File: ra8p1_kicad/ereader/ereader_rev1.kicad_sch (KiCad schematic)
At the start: 0 parts

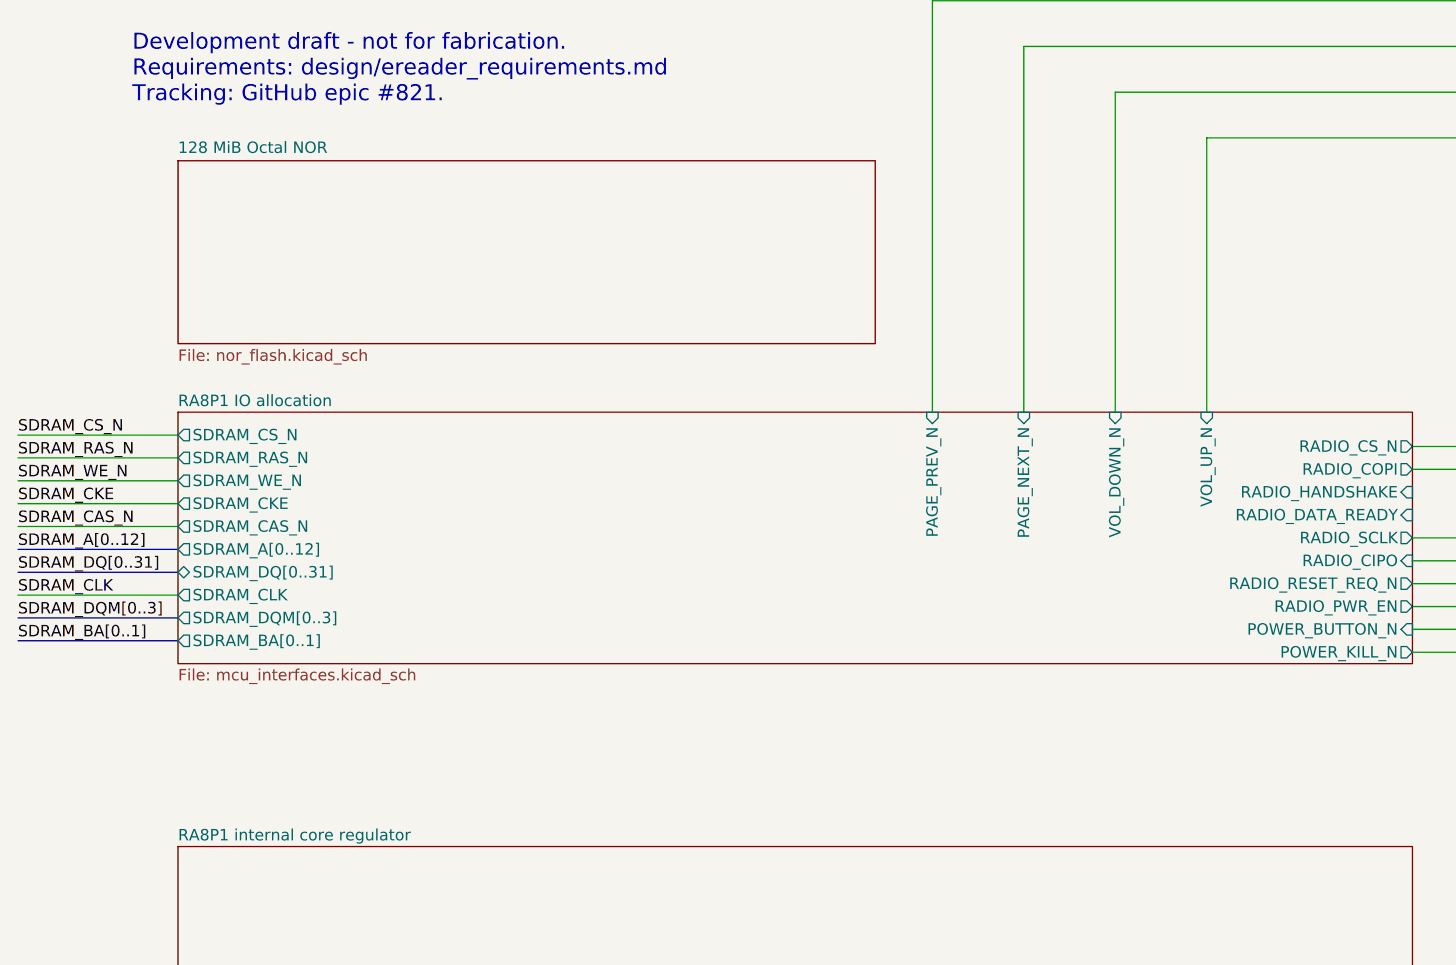
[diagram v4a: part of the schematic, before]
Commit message: Connect Octal NOR hierarchy and configured MCU pins
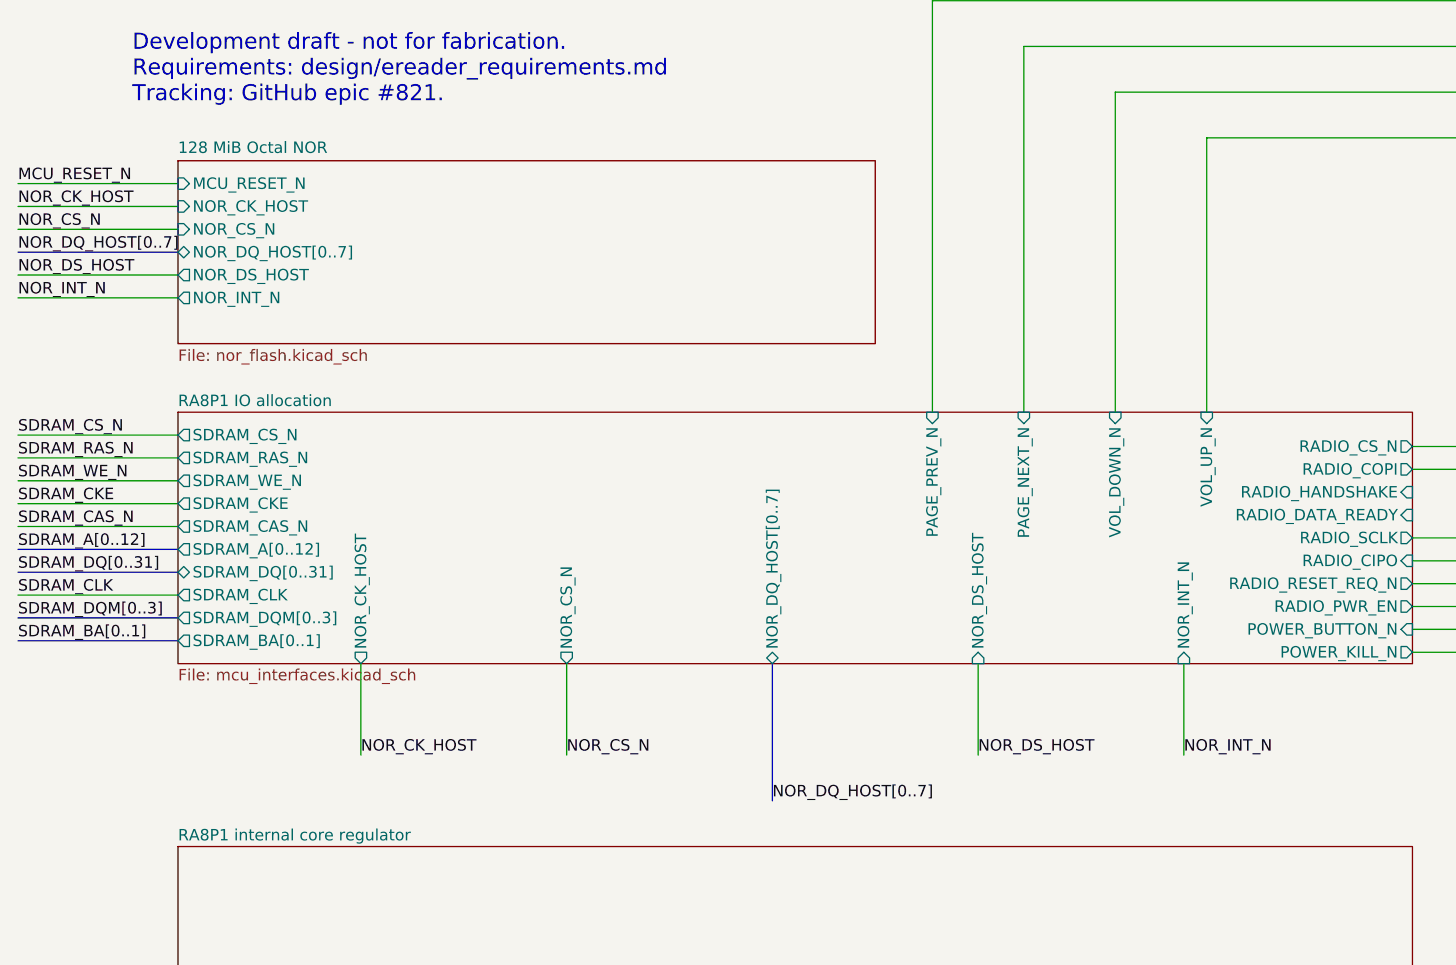
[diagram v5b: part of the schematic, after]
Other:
- sheet 128 MiB Octal NOR ports: added MCU_RESET_N, NOR_CK_HOST, NOR_CS_N, NOR_DQ_HOST[0..7], NOR_DS_HOST, NOR_INT_N; removed none
- sheet RA8P1 IO allocation ports: added NOR_CK_HOST, NOR_CS_N, NOR_DQ_HOST[0..7], NOR_DS_HOST, NOR_INT_N; removed none

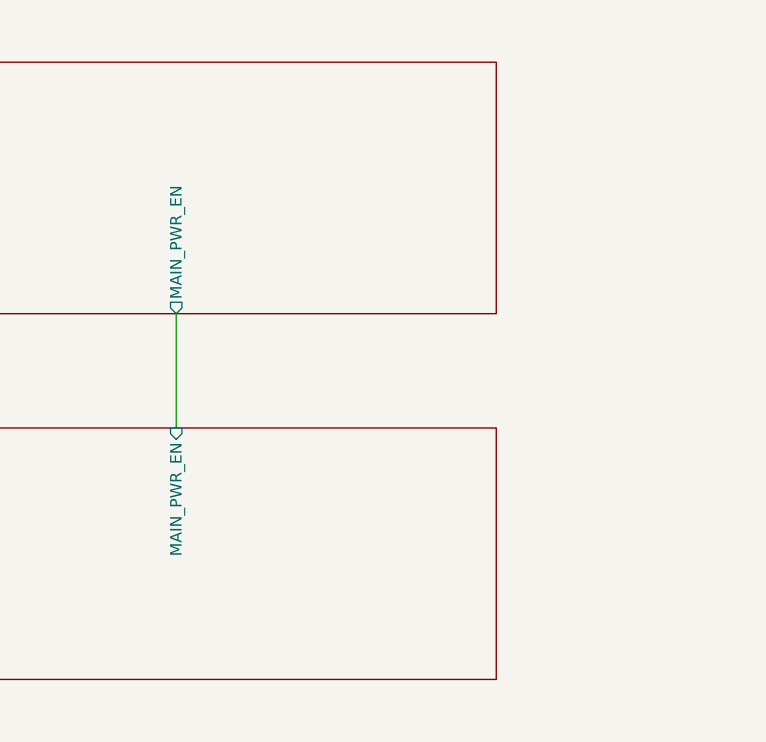
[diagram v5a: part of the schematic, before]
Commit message: Wire LTC3119 power-stage draft and held RUN control
Add native RUN buffer and held-domain clamp with verified connectivity, sourced BOM fields, and linked PWR-004 calculations. Export the full schematic PDF and native BOM.

Keep rail adoption blocked by SDRAM logic-high conflict #846. Whole-project ERC remains 133 errors and two warnings; this checkpoint adds no findings.
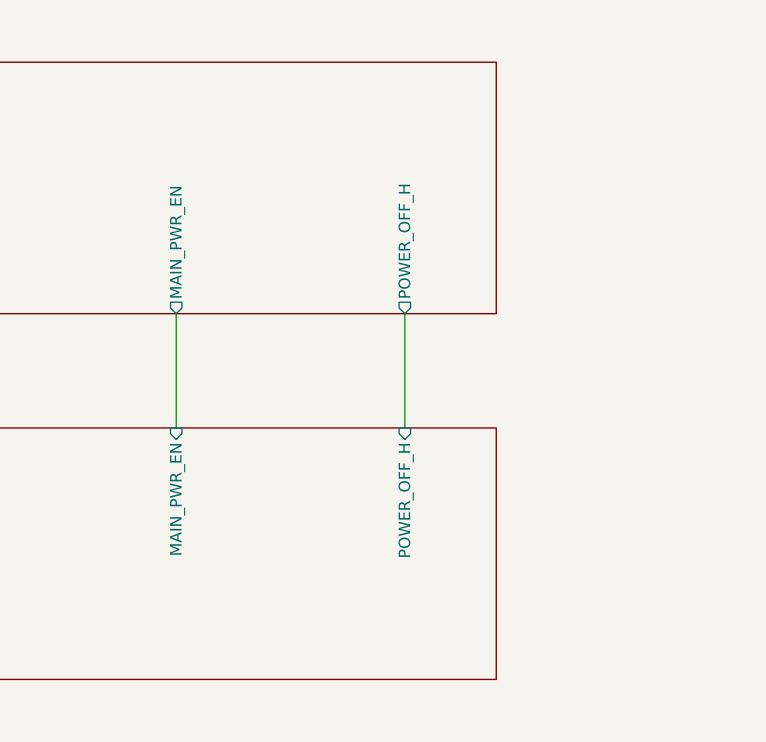
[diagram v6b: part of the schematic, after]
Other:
- sheet Main 3V3 digital supply ports: added POWER_OFF_H; removed none
- sheet Power button and source control ports: added POWER_OFF_H; removed none
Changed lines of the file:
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@@
+	(wire
+		(pts
+			(xy 330.2 205.74) (xy 330.2 218.44)
+		)
+		(stroke
+			(width 0)
+			(type default)
+		)
+	)
 	(wire
 		(pts
@@
 			)
 		)
+		(pin "POWER_OFF_H" input
+			(at 330.2 218.44 90)
+			(effects
+				(font
+					(size 1.27 1.27)
+				)
+				(justify right)
+			)
+		)
 		(instances
 			(project "ereader_rev1"
@@
 			(effects
 				(font
+					(size 1.27 1.27)
+				)
+				(justify left)
+			)
+		)
+		(pin "POWER_OFF_H" output
+			(at 330.2 205.74 270)
+			(effects
+				(font

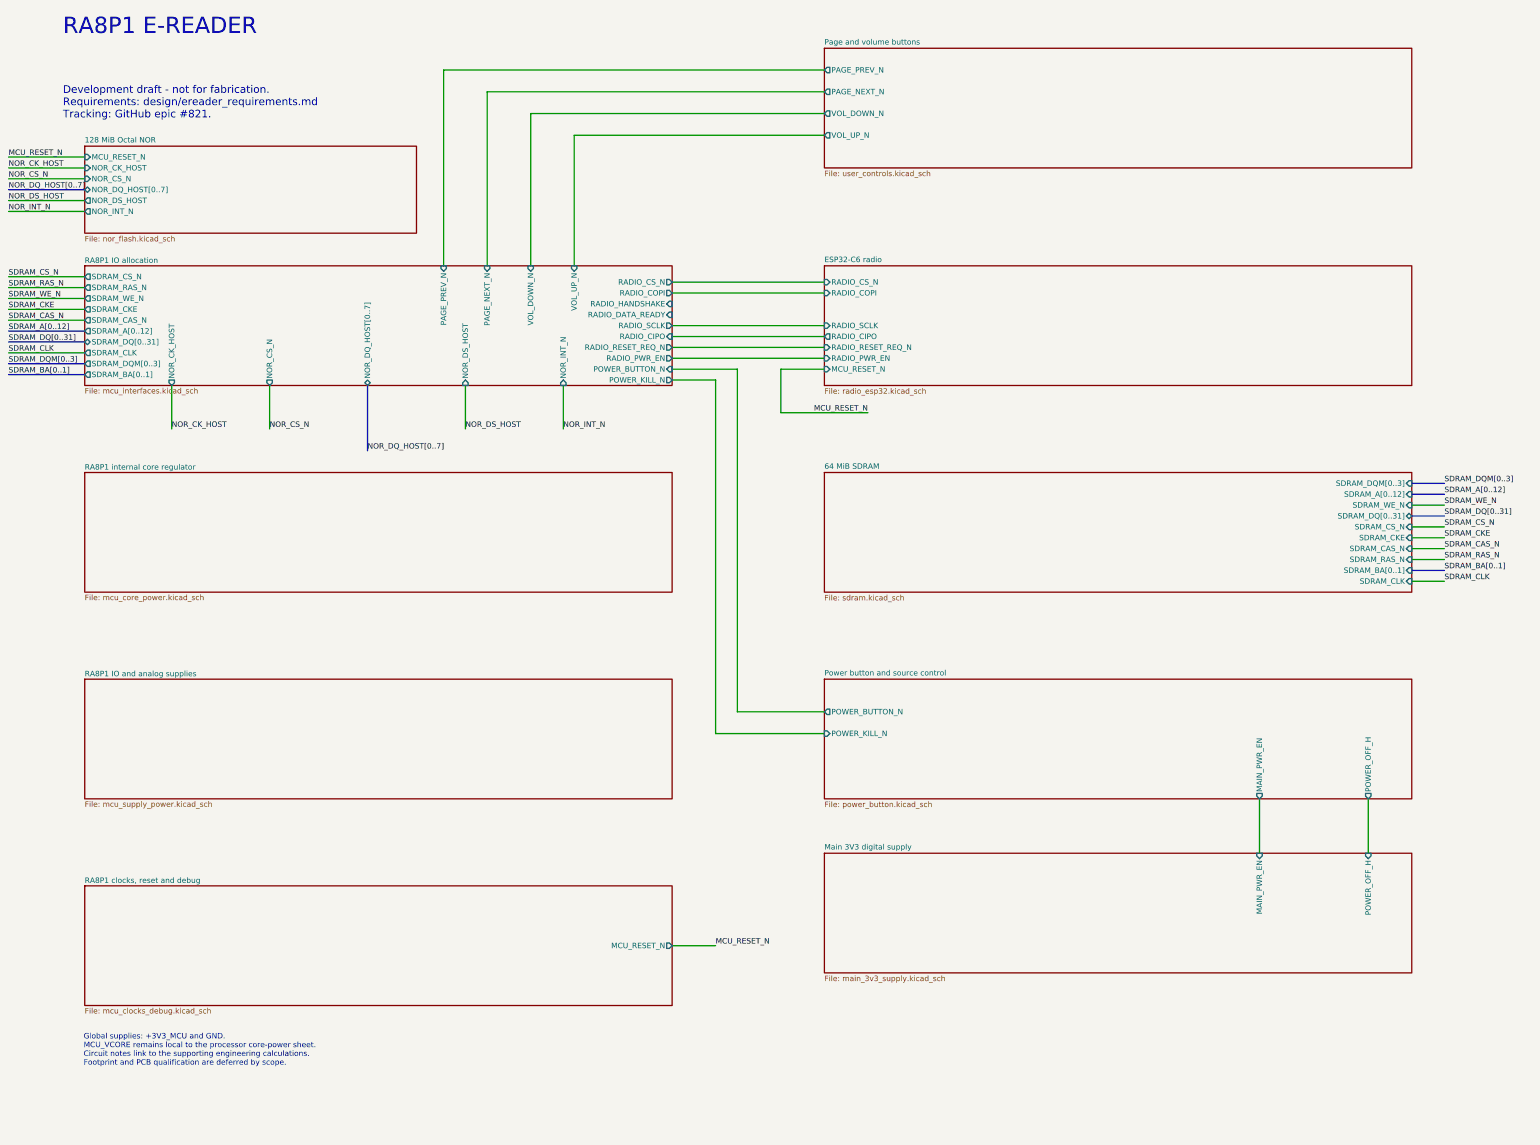
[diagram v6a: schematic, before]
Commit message: Add microSD socket and verified mechanical card detect
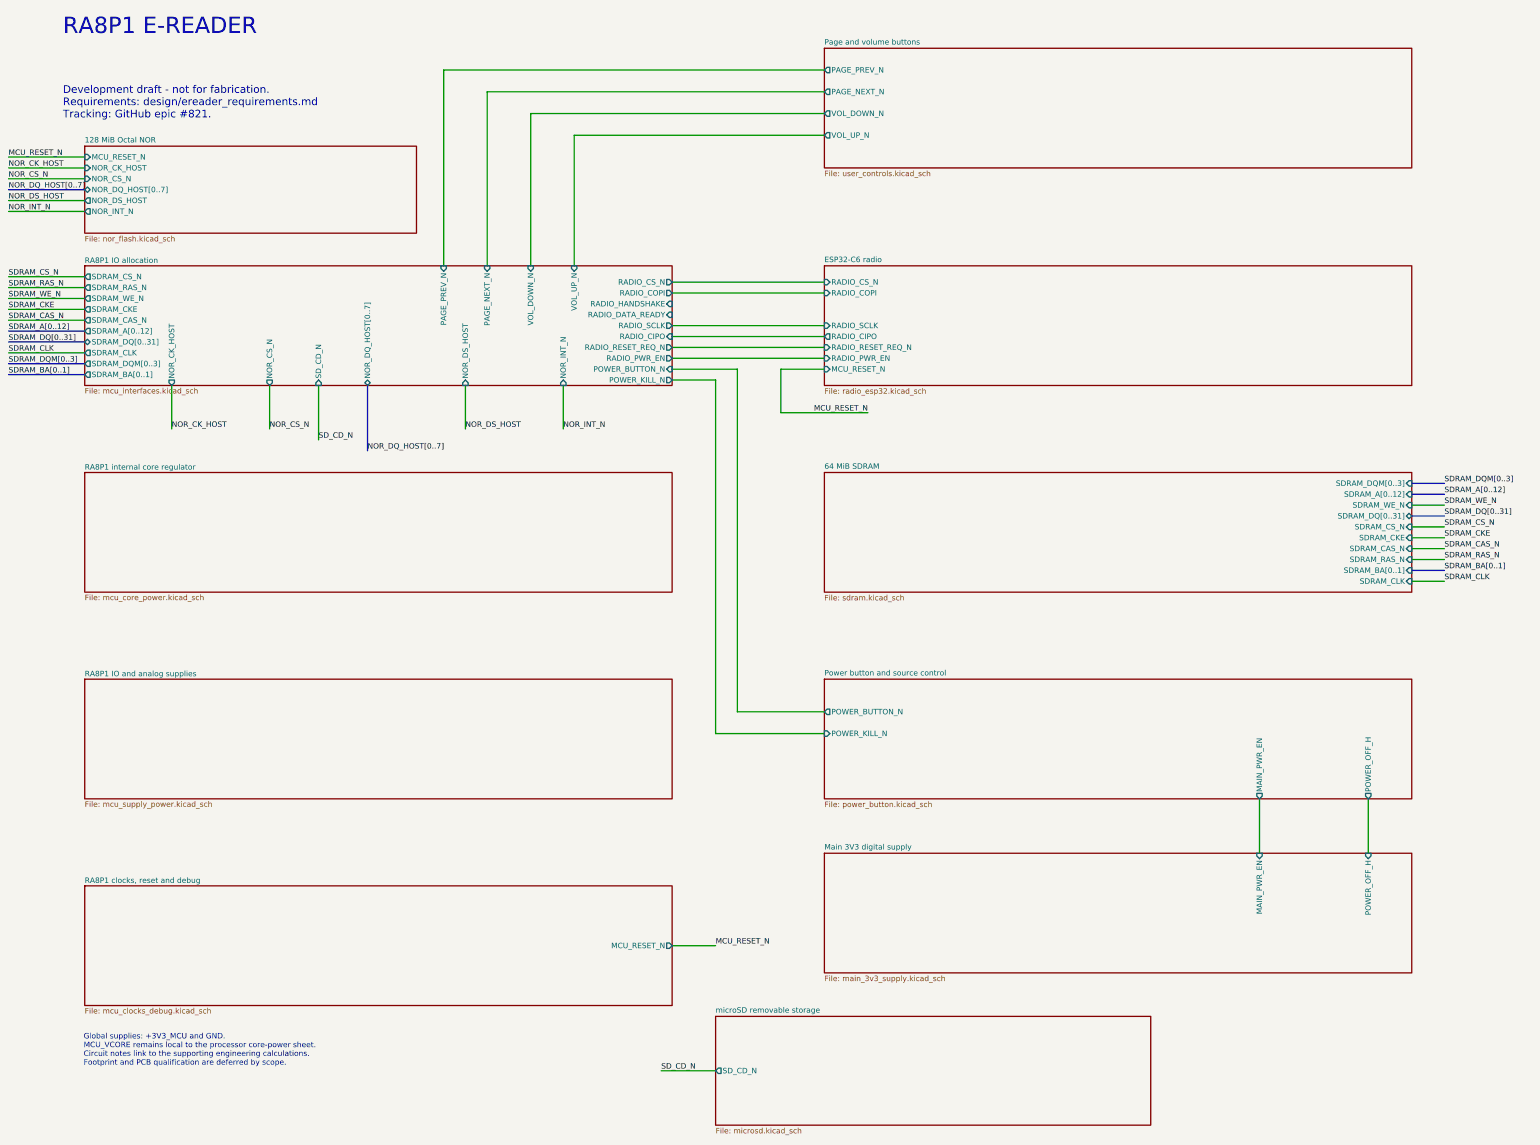
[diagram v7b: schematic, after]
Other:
- added sheet microSD removable storage (microsd.kicad_sch)
- sheet RA8P1 IO allocation ports: added SD_CD_N; removed none
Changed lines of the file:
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@@
+	(wire
+		(pts
+			(xy 85.09 109.22) (xy 85.09 121.92)
+		)
+		(stroke
+			(width 0)
+			(type default)
+		)
+	)
 	(wire
 		(pts
@@
 		(pts
 			(xy 12.7 58.42) (xy 30.48 58.42)
+		)
+		(stroke
+			(width 0)
+			(type default)
+		)
+	)
+	(wire
+		(pts
+			(xy 165.1 269.24) (xy 177.8 269.24)
 		)
 		(stroke
@@
 		)
 	)
+	(label "SD_CD_N"
+		(at 85.09 121.92 0)
+		(effects
+			(font
+				(size 1.27 1.27)
+			)
+			(justify left bottom)
+		)
+	)
 	(label "SDRAM_BA[0..1]"
 		(at 347.98 152.4 0)
@@
 	(label "SDRAM_DQM[0..3]"
 		(at 12.7 104.14 0)
+		(effects
+			(font
+				(size 1.27 1.27)
+			)
+			(justify left bottom)
+		)
+	)
+	(label "SD_CD_N"
+		(at 165.1 269.24 0)
 		(effects
 			(font
@@
 			)
 		)
+		(pin "SD_CD_N" input
+			(at 85.09 109.22 270)
+			(effects
+				(font
+					(size 1.27 1.27)
+				)
+				(justify left)
+			)
+		)
 		(instances
 			(project "ereader_rev1"
@@
 				)
 			)
+		)
+	)
+	(sheet
+		(at 177.8 256.54)
+		(size 101.6 25.4)
+		(exclude_from_sim no)
+		(in_bom yes)
+		(on_board yes)
+		(dnp no)
+		(fields_autoplaced yes)
+		(stroke
+			(width 0.1524)
+			(type solid)
+		)
+		(fill
+			(color 0 0 0 0)
+		)
+		(property "Sheetname" "microSD removable storage"
+			(at 177.8 255.8284 0)
+			(show_name no)
+			(do_not_autoplace no)
+			(effects
+				(font
+					(size 1.27 1.27)
+				)
+				(justify left bottom)
+			)
+		)
+		(property "Sheetfile" "microsd.kicad_sch"
+			(at 177.8 282.5246 0)
+			(show_name no)
+			(do_not_autoplace no)
+			(effects
+				(font
+					(size 1.27 1.27)
+				)
+				(justify left top)
+			)
+		)
+		(pin "SD_CD_N" output
+			(at 177.8 269.24 180)
+			(effects
+				(font
+					(size 1.27 1.27)
+				)
+				(justify left)
+			)
+		)
+		(instances
+			(project "ereader_rev1"
+				(path "/0586cc51-9c57-495b-a0c9-c29ba0d48166"
+					(page "12")
+				)
+			)

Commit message: hardware: integrate supervised microSD power and SDHI bus (#827, #845, #846)
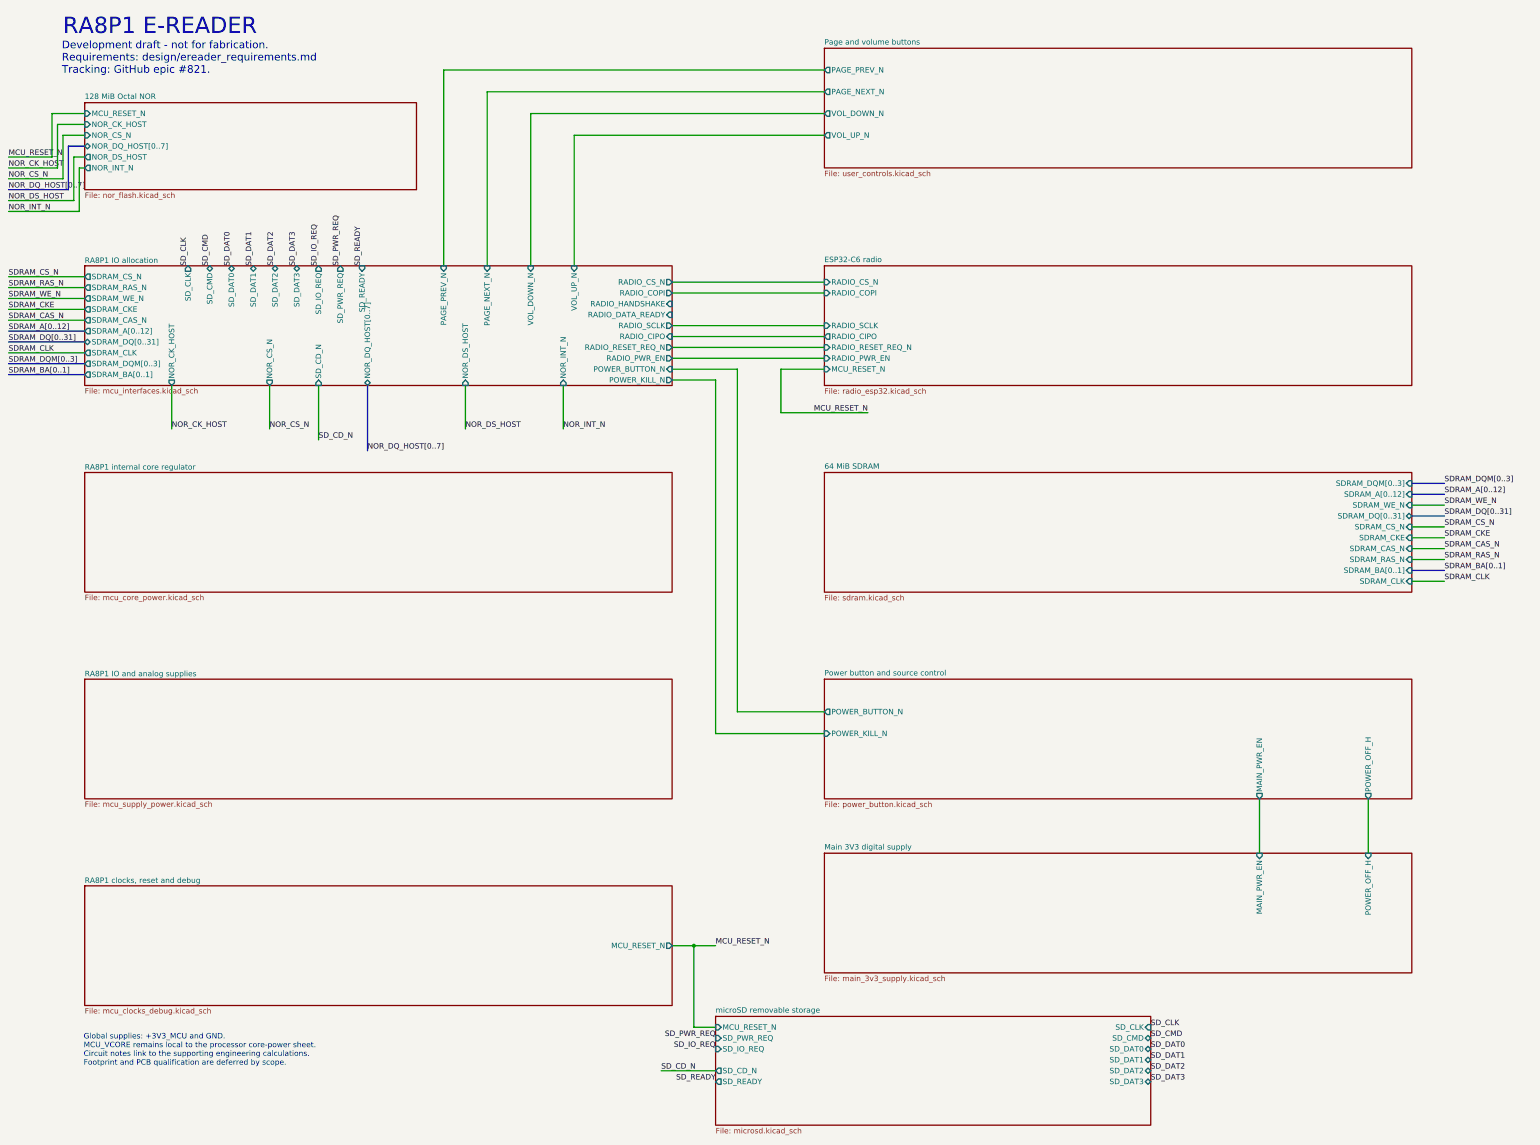
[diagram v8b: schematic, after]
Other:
- sheet RA8P1 IO allocation ports: added SD_CLK, SD_CMD, SD_DAT0, SD_DAT1, SD_DAT2, SD_DAT3, SD_IO_REQ, SD_PWR_REQ, SD_READY; removed none
- sheet microSD removable storage ports: added MCU_RESET_N, SD_CLK, SD_CMD, SD_DAT0, SD_DAT1, SD_DAT2, SD_DAT3, SD_IO_REQ, SD_PWR_REQ, SD_READY; removed none
